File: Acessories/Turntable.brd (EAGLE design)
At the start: 80 x 50 mm, 34 parts, among them IC1 7812TV, IC2 7805TV, M1 ARDUINO-NANO-3.0, U2 A4988, X1 MKDSN1,5/4-5,08, X2 1751248, X3 1751264

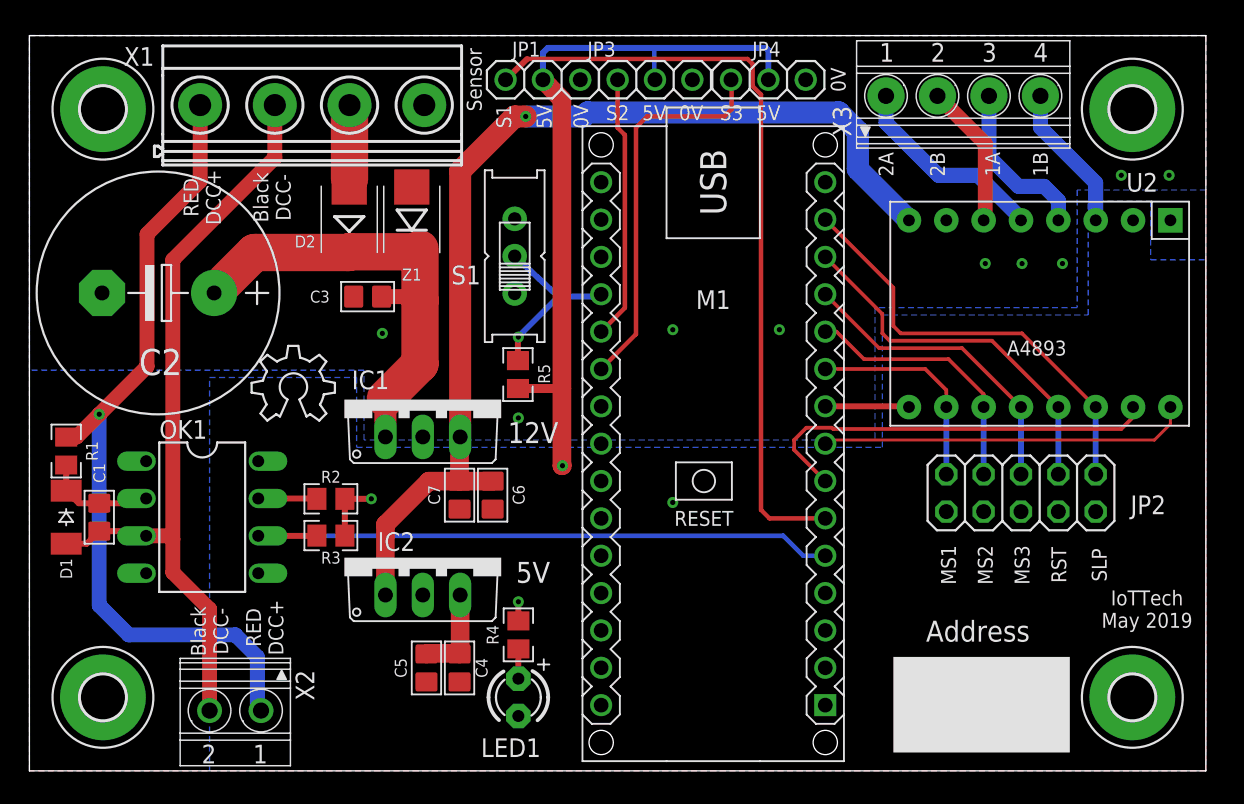
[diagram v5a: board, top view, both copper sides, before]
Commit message: Added connector for external stepper drive
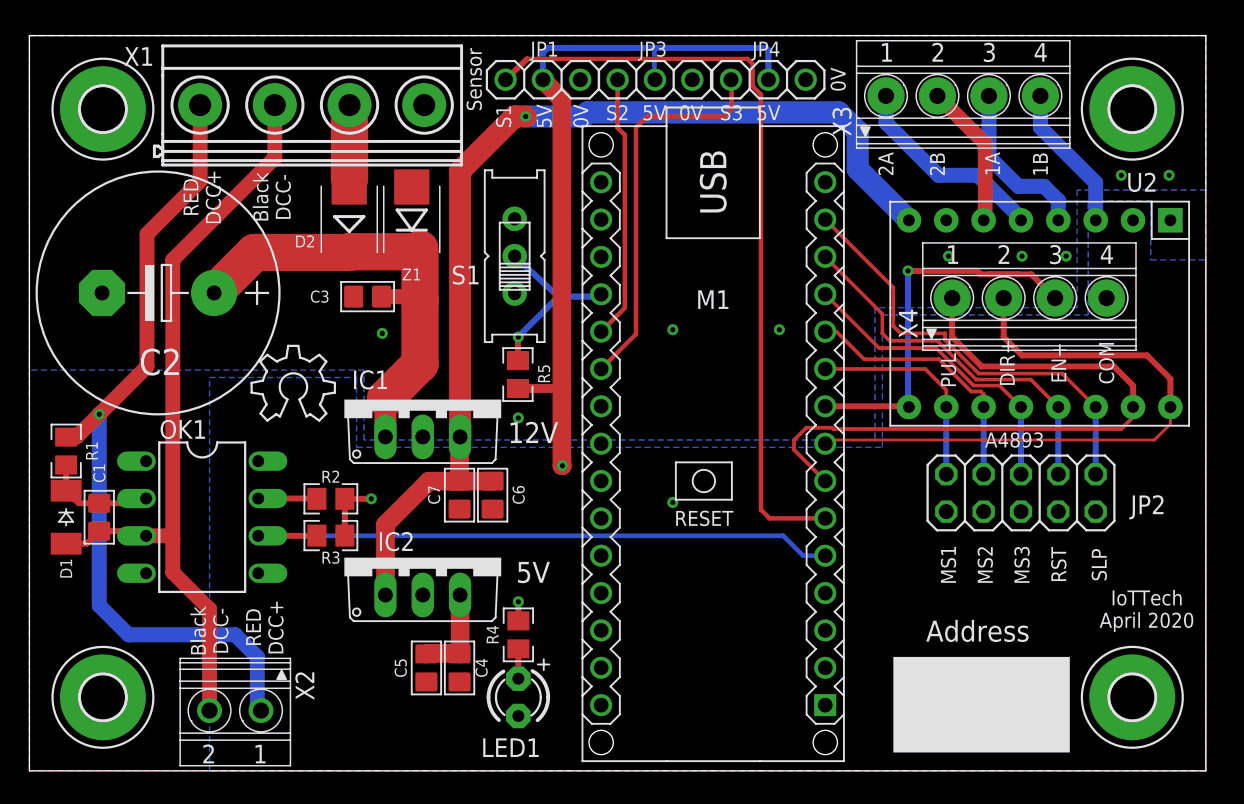
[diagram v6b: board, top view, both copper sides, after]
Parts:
- added X4: 1751264, con-phoenix-350:1751264
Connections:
- net DIR: now also X4.2
- net GND: now also X4.4
- net M-EN: now also X4.3
- net STEP: now also X4.1
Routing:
- net M-EN: track 5.71 -> 25.8 mm, vias 0 -> 1
- net STEP: track 28.1 -> 45.9 mm
- net DIR: track 25.2 -> 42.3 mm
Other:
- board text added: "COM"
- board text added: "DIR+"
- board text added: "EN+"
- board text added: "IoTTech April 2020"
- board text added: "PUL+"
- board text removed: "IoTTech May 2019"
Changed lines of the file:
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@@
 <?xml version="1.0" encoding="utf-8"?>
 <!DOCTYPE eagle SYSTEM "eagle.dtd">
-<eagle version="9.4.2">
+<eagle version="9.6.0">
 <drawing>
 <settings>
@@
 <text x="30" y="-11" size="1.016" layer="21" rot="R90" align="center">RST</text>
 <text x="32.75" y="-11" size="1.016" layer="21" rot="R90" align="center">SLP</text>
-<text x="28.5" y="3.75" size="1.016" layer="21" align="center">A4893</text>
+<text x="27" y="-2.5" size="1.016" layer="21" align="center">A4893</text>
 <text x="-5.75" y="-11.5" size="1.4224" layer="21" align="center">5V</text>
 <text x="-5.75" y="-2" size="1.4224" layer="21" align="center">12V</text>
@@
 DCC-</text>
 <text x="36" y="-14" size="1.016" layer="21" align="center">IoTTech
-May 2019</text>
+April 2020</text>
 <text x="-7.75" y="19.5" size="1.016" layer="21" rot="R90" align="center">S1</text>
 <text x="-5" y="19.5" size="1.016" layer="21" rot="R90" align="center">5V</text>
@@
 <text x="0" y="19.75" size="1.016" layer="21" rot="R180" align="center">S2</text>
 <text x="7.75" y="19.75" size="1.016" layer="21" rot="R180" align="center">S3</text>
+<text x="22.5" y="2.75" size="1.016" layer="21" rot="R90" align="center">PUL+</text>
+<text x="26.5" y="2.75" size="1.016" layer="21" rot="R90" align="center">DIR+</text>
+<text x="30" y="2.75" size="1.016" layer="21" rot="R90" align="center">EN+</text>
+<text x="33.25" y="2.75" size="1.016" layer="21" rot="R90" align="center">COM</text>
 </plain>
 <attributes>
@@
 <element name="H4" library="holes" package="3,0-PAD" value="MOUNT-PAD-ROUND3.0" x="-35" y="20" smashed="yes"/>
 <element name="JP1" library="adafruit" library_urn="urn:adsk.eagle:library:420" package="1X03" package3d_urn="urn:adsk.eagle:package:6240710/1" value="" x="-5.08" y="22" smashed="yes">
-<attribute name="NAME" x="-6.2162" y="24.0788" size="1.016" layer="25" ratio="10" align="center"/>
+<attribute name="NAME" x="-4.9662" y="24.0788" size="1.016" layer="25" ratio="10" align="center"/>
 <attribute name="VALUE" x="-8.89" y="18.825" size="1.27" layer="27"/>
 </element>
@@
 </element>
 <element name="JP3" library="adafruit" library_urn="urn:adsk.eagle:library:420" package="1X03" package3d_urn="urn:adsk.eagle:package:6240710/1" value="" x="2.54" y="22" smashed="yes">
-<attribute name="NAME" x="-1.0962" y="24.0788" size="1.016" layer="25" ratio="10" align="center"/>
+<attribute name="NAME" x="2.4038" y="24.0788" size="1.016" layer="25" ratio="10" align="center"/>
 <attribute name="VALUE" x="-1.27" y="18.825" size="1.27" layer="27"/>
 </element>
@@
 <attribute name="NAME" x="10.1138" y="24.0788" size="1.016" layer="25" ratio="10" align="center"/>
 <attribute name="VALUE" x="6.44" y="18.825" size="1.27" layer="27"/>
+</element>
+<element name="X4" library="con-phoenix-350" package="1751264" value="1751264" x="28" y="7.25" smashed="yes">
+<attribute name="MF" value="" x="28" y="7.25" size="1.778" layer="27" display="off"/>
+<attribute name="MPN" value="1751264" x="28" y="7.25" size="1.778" layer="27" display="off"/>
+<attribute name="NAME" x="20.395" y="4.3925" size="1.27" layer="25" rot="R90"/>
+<attribute name="OC_FARNELL" value="unknown" x="28" y="7.25" size="1.778" layer="27" display="off"/>
+<attribute name="OC_NEWARK" value="10R0934" x="28" y="7.25" size="1.778" layer="27" display="off"/>
+<attribute name="VALUE" x="27.6975" y="11.3775" size="1.27" layer="27"/>
 </element>
 </elements>
@@
 <via x="-16" y="4.75" extent="1-16" drill="0.35"/>
 <via x="3.75" y="-6.75" extent="1-16" drill="0.35"/>
-<via x="25" y="9.5" extent="1-16" drill="0.35"/>
-<via x="27.5" y="9.5" extent="1-16" drill="0.35"/>
-<via x="30.25" y="9.5" extent="1-16" drill="0.35"/>
+<via x="22.5" y="10" extent="1-16" drill="0.35"/>
+<via x="27.5" y="10" extent="1-16" drill="0.35"/>
+<via x="30.5" y="10" extent="1-16" drill="0.35"/>
 <contactref element="C6" pad="2"/>
 <contactref element="C7" pad="2"/>
@@
 <contactref element="JP1" pad="3"/>
 <contactref element="JP4" pad="3"/>
+<contactref element="X4" pad="4"/>
 </signal>
 <signal name="+5V">
@@
 <wire x1="14.12" y1="-0.21" x2="19.76" y2="-0.21" width="0.4064" layer="1"/>
 <wire x1="19.76" y1="-0.21" x2="19.81" y2="-0.26" width="0.4064" layer="1"/>
+<contactref element="X4" pad="3"/>
+<wire x1="25.30395" y1="8.7662" x2="24.69605" y2="8.7662" width="0.4064" layer="1"/>
+<wire x1="24.69605" y1="8.7662" x2="24.46225" y2="9" width="0.4064" layer="1"/>
+<wire x1="24.46225" y1="9" x2="19.75" y2="9" width="0.4064" layer="1"/>
+<wire x1="29.75" y1="7.15" x2="28.1338" y2="8.7662" width="0.4064" layer="1"/>
+<wire x1="28.1338" y1="8.7662" x2="27.19605" y2="8.7662" width="0.4064" layer="1"/>
+<wire x1="27.19605" y1="8.7662" x2="27.18665" y2="8.7756" width="0.4064" layer="1"/>
+<wire x1="27.18665" y1="8.7756" x2="25.31335" y2="8.7756" width="0.4064" layer="1"/>
+<wire x1="25.31335" y1="8.7756" x2="25.30395" y2="8.7662" width="0.4064" layer="1"/>
+<via x="19.75" y="9" extent="1-16" drill="0.35"/>
+<wire x1="19.75" y1="9" x2="19.75" y2="-0.2" width="0.4064" layer="16"/>
+<wire x1="19.75" y1="-0.2" x2="19.81" y2="-0.26" width="0.4064" layer="16"/>
 </signal>
 <signal name="POS1">
@@
 <wire x1="35.05" y1="-0.95" x2="35.05" y2="-0.26" width="0.254" layer="1"/>
 <wire x1="12" y1="-2.5" x2="12.8342" y2="-1.6658" width="0.254" layer="1"/>
+<contactref element="X4" pad="1"/>
+<wire x1="22.75" y1="7.15" x2="22.75" y2="4.5" width="0.4064" layer="1"/>
+<wire x1="35.05" y1="1.2" x2="35.05" y2="-0.26" width="0.4064" layer="1"/>
+<wire x1="22.75" y1="4.5" x2="24.75" y2="2.5" width="0.4064" layer="1"/>
+<wire x1="24.75" y1="2.5" x2="33.75" y2="2.5" width="0.4064" layer="1"/>
+<wire x1="33.75" y1="2.5" x2="35.05" y2="1.2" width="0.4064" layer="1"/>
 </signal>
 <signal name="DIR">
@@
 <wire x1="14.37" y1="-2.5" x2="36.5" y2="-2.5" width="0.2032" layer="1"/>
 <wire x1="36.5" y1="-2.5" x2="37.59" y2="-1.41" width="0.2032" layer="1"/>
+<contactref element="X4" pad="2"/>
+<wire x1="26.25" y1="7.15" x2="26.25" y2="4.5" width="0.4064" layer="1"/>
+<wire x1="37.59" y1="1.66" x2="37.59" y2="-0.26" width="0.4064" layer="1"/>
+<wire x1="26.25" y1="4.5" x2="27.5" y2="3.25" width="0.4064" layer="1"/>
+<wire x1="27.5" y1="3.25" x2="36" y2="3.25" width="0.4064" layer="1"/>
+<wire x1="36" y1="3.25" x2="37.59" y2="1.66" width="0.4064" layer="1"/>
 </signal>
 <signal name="LEARN">
@@
 <wire x1="24.89" y1="-4.83" x2="24.89" y2="-0.26" width="0.4064" layer="16"/>
 <wire x1="14.12" y1="4.87" x2="14.88" y2="4.87" width="0.254" layer="1"/>
-<wire x1="16.75" y1="3" x2="22.5" y2="3" width="0.254" layer="1"/>
-<wire x1="22.5" y1="3" x2="24.89" y2="0.61" width="0.254" layer="1"/>
 <wire x1="24.89" y1="0.61" x2="24.89" y2="-0.26" width="0.254" layer="1"/>
 <wire x1="14.88" y1="4.87" x2="16.75" y2="3" width="0.254" layer="1"/>
+<wire x1="16.75" y1="3" x2="21.8432875" y2="3" width="0.254" layer="1"/>
+<wire x1="24.0450875" y1="0.7982" x2="24.7018" y2="0.7982" width="0.254" layer="1"/>
+<wire x1="24.7018" y1="0.7982" x2="24.89" y2="0.61" width="0.254" layer="1"/>
+<wire x1="21.8432875" y1="3" x2="24.0450875" y2="0.7982" width="0.254" layer="1"/>
 </signal>
 <signal name="MS3">
@@
 <wire x1="27.43" y1="-4.83" x2="27.43" y2="-0.26" width="0.4064" layer="16"/>
 <wire x1="14.12" y1="7.41" x2="17.78" y2="3.75" width="0.254" layer="1"/>
-<wire x1="23.42" y1="3.75" x2="27.43" y2="-0.26" width="0.254" layer="1"/>
-<wire x1="17.78" y1="3.75" x2="23.42" y2="3.75" width="0.254" layer="1"/>
+<wire x1="17.78" y1="3.75" x2="21.668025" y2="3.75" width="0.254" layer="1"/>
+<wire x1="24.213425" y1="1.2046" x2="25.9654" y2="1.2046" width="0.254" layer="1"/>
+<wire x1="25.9654" y1="1.2046" x2="27.43" y2="-0.26" width="0.254" layer="1"/>
+<wire x1="21.668025" y1="3.75" x2="24.213425" y2="1.2046" width="0.254" layer="1"/>
 </signal>
 <signal name="!RESET">
@@
 <wire x1="18" y1="6.07" x2="18" y2="4.75" width="0.254" layer="1"/>
 <wire x1="18" y1="4.75" x2="18.5" y2="4.25" width="0.254" layer="1"/>
-<wire x1="25.46" y1="4.25" x2="29.97" y2="-0.26" width="0.254" layer="1"/>
-<wire x1="18.5" y1="4.25" x2="25.46" y2="4.25" width="0.254" layer="1"/>
+<wire x1="18.5" y1="4.25" x2="21.7427625" y2="4.25" width="0.254" layer="1"/>
+<wire x1="24.3817625" y1="1.611" x2="28.099" y2="1.611" width="0.254" layer="1"/>
+<wire x1="28.099" y1="1.611" x2="29.97" y2="-0.26" width="0.254" layer="1"/>
+<wire x1="21.7427625" y1="4.25" x2="24.3817625" y2="1.611" width="0.254" layer="1"/>
 </signal>
 <signal name="!SLEEP">
@@
 <wire x1="18.75" y1="7.86" x2="18.75" y2="5.25" width="0.254" layer="1"/>
 <wire x1="18.75" y1="5.25" x2="19.25" y2="4.75" width="0.254" layer="1"/>
-<wire x1="27.5" y1="4.75" x2="32.51" y2="-0.26" width="0.254" layer="1"/>
-<wire x1="19.25" y1="4.75" x2="27.5" y2="4.75" width="0.254" layer="1"/>
+<wire x1="19.25" y1="4.75" x2="22.2674" y2="4.75" width="0.254" layer="1"/>
+<wire x1="22.2674" y1="4.75" x2="22.2674" y2="4.3001" width="0.254" layer="1"/>
+<wire x1="24.5501" y1="2.0174" x2="30.2326" y2="2.0174" width="0.254" layer="1"/>
+<wire x1="30.2326" y1="2.0174" x2="32.51" y2="-0.26" width="0.254" layer="1"/>
+<wire x1="22.2674" y1="4.3001" x2="24.5501" y2="2.0174" width="0.254" layer="1"/>
 </signal>
 <signal name="POS2">
